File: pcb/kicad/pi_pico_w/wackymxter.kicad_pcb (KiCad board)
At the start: 2 copper layers, 165.9 x 126.4 mm, 73 parts, among them J1 OLED_128x32, U1 RP2040_Zero, U3 TRRS

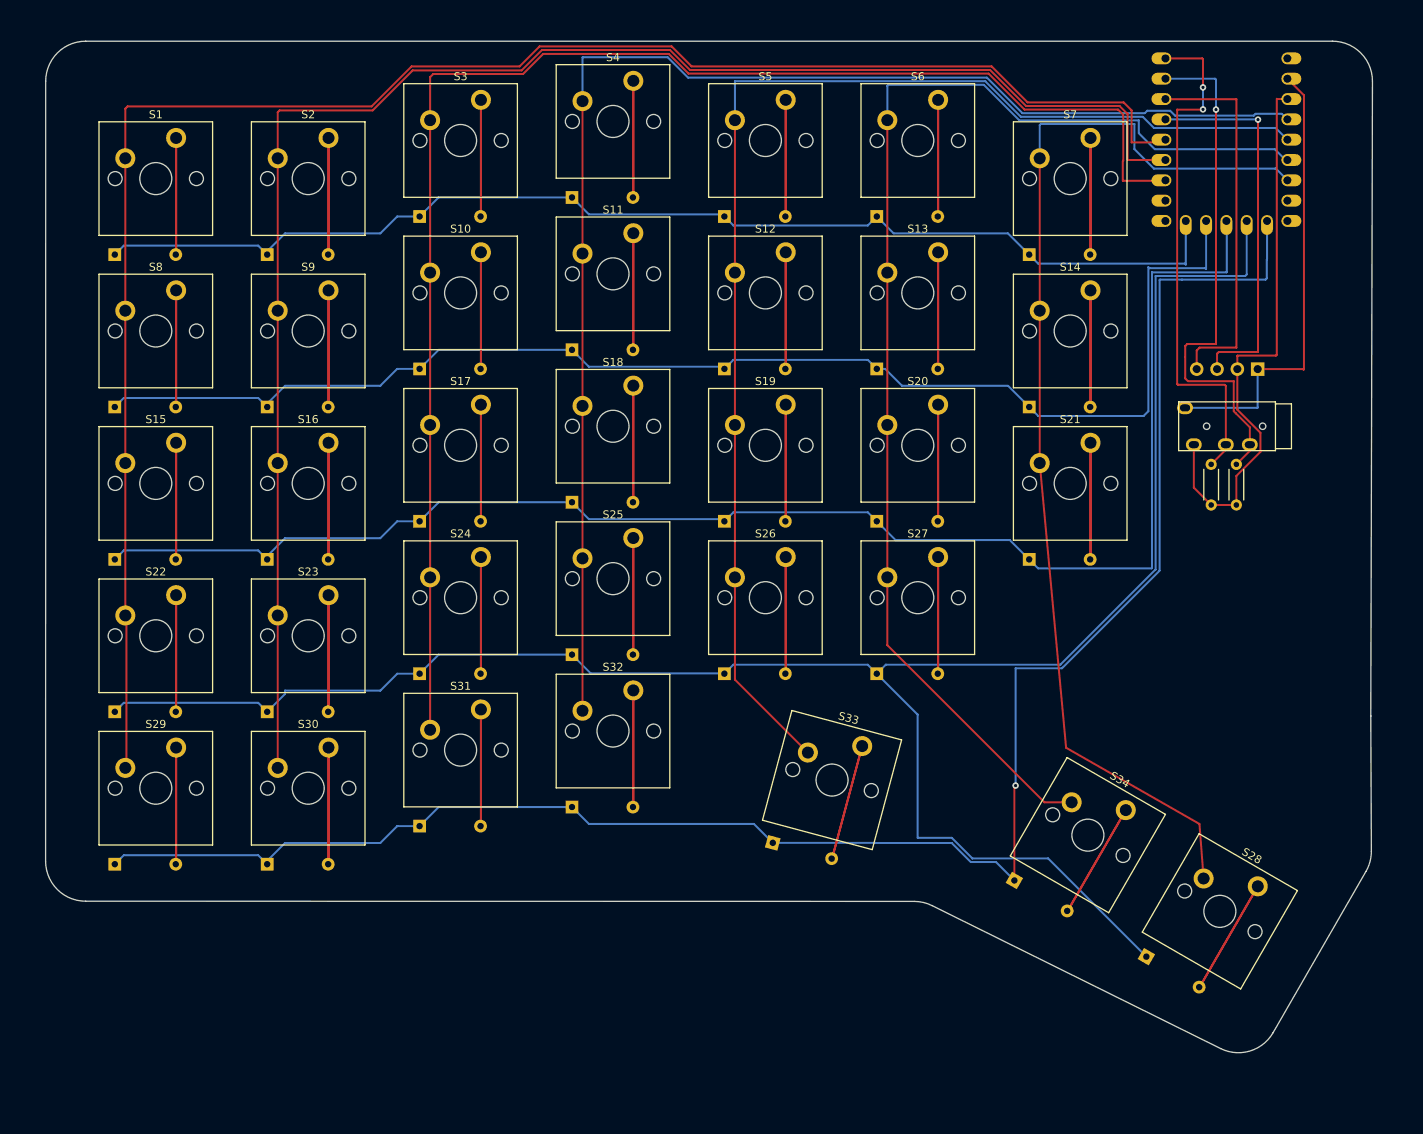
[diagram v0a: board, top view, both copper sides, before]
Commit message: [KiCAD] Pi Pico W with LEDs and Rotary Encoder
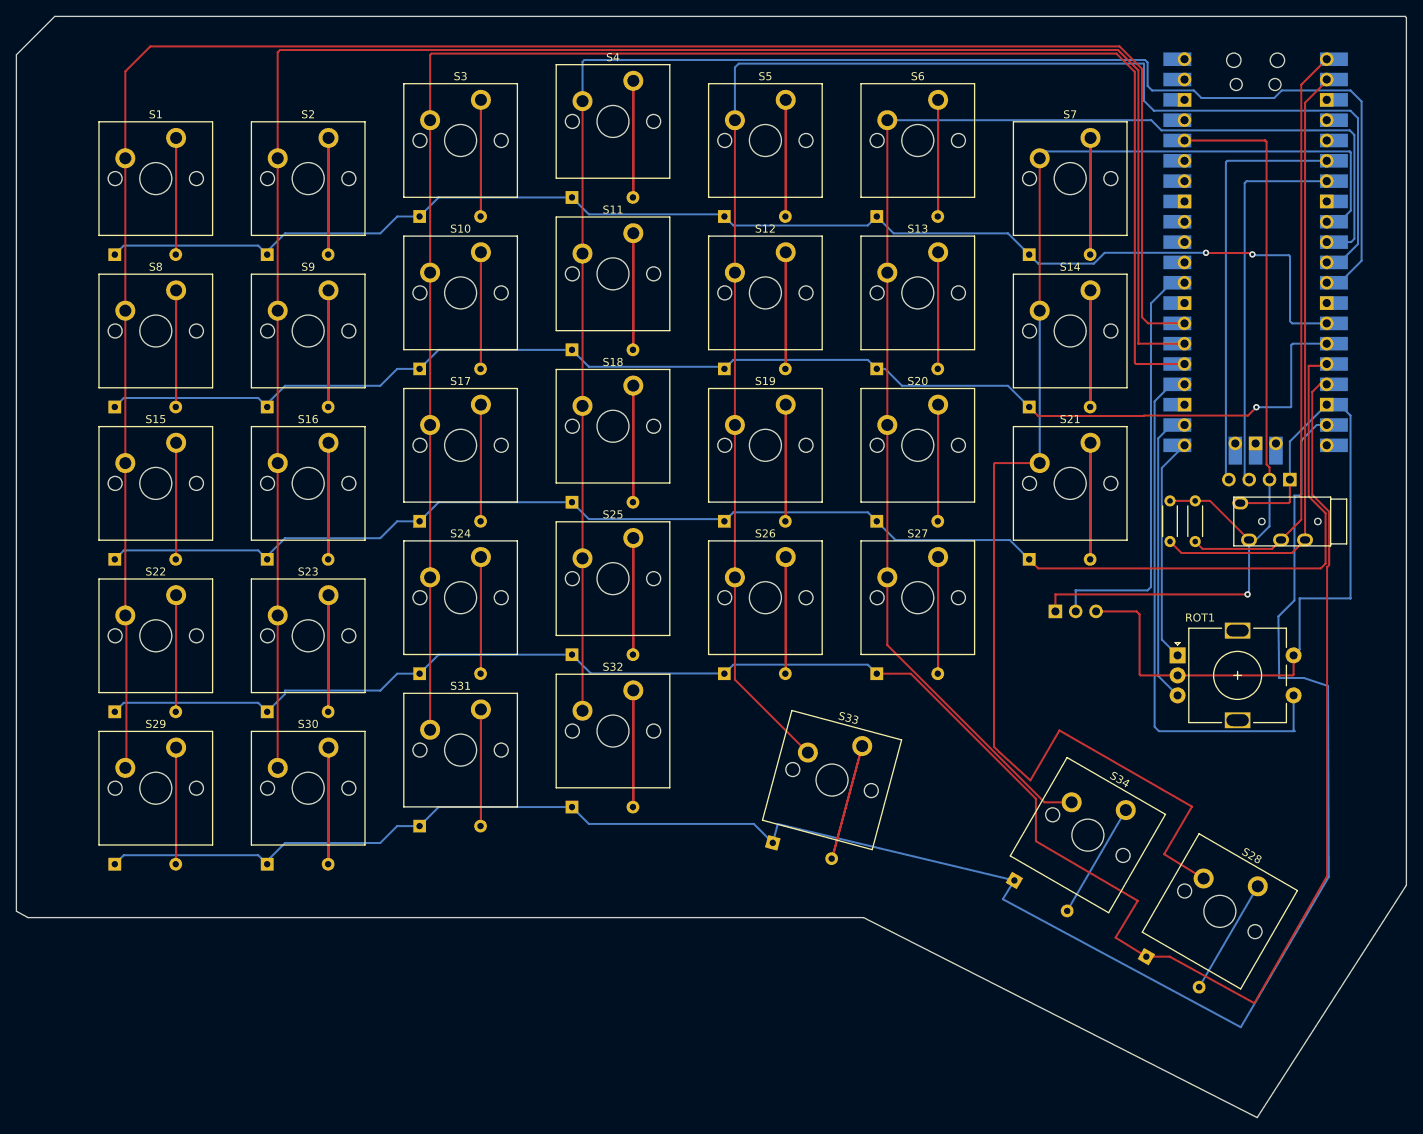
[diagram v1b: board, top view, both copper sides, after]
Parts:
- added J2: Conn_01x03, Connector_PinHeader_2.54mm:PinHeader_1x03_P2.54mm_Horizontal, B.Cu at (156.5, 95.8)
- added ROT1: RotaryEncoder_Switch, Rotary_Encoder:RotaryEncoder_Alps_EC11E-Switch_Vertical_H20mm, F.Cu at (171.8, 101.3)
- U1: value RP2040_Zero -> Pico; footprint ScottoKeebs_MCU:RP2040_Zero -> MCU_RaspberryPi_and_Boards:RPi_Pico_SMD_TH
- moved U1 14.5 mm to (181.5, 50.9)
- moved J1 14.4 mm to (176.0, 80.9)
- moved U3 13.8 mm to (190.9, 84.5)
- moved R2 8.31 mm to (170.8, 82.0), turned to -90 degrees
- moved R1 2.06 mm to (174.0, 82.0), turned to -90 degrees
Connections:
- U1 pad 10: row0 -> col5
- U1 pad 11: row1 -> col4
- U1 pad 12: row2 -> col3
- U1 pad 13: row3 -> unconnected-(U1-GND-Pad13)
- U1 pad 14: row4 -> row0
- U1 pad 15: unconnected-(U1-14-Pad15) -> row1
- U1 pad 16: unconnected-(U1-15-Pad16) -> row2
- U1 pad 17: col6 -> row3
- U1 pad 18: col5 -> GND
- U1 pad 19: col4 -> row4
- U1 pad 20: col3 -> unconnected-(U1-GPIO15-Pad20)
- U1 pad 21: VCC -> ROT1
- U1 pad 22: GND -> ROT2
- U1 pad 3: SDA -> unconnected-(U1-GND-Pad3)
- U1 pad 4: SCL -> unconnected-(U1-GPIO2-Pad4)
- U1 pad 5: col0 -> unconnected-(U1-GPIO3-Pad5)
- U1 pad 6: col1 -> SDA
- U1 pad 7: col2 -> SCL
- U1 pad 9: unconnected-(U1-8-Pad9) -> col6
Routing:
- net B1: track 0.00 -> 67.6 mm
- net LED1: track 0.00 -> 52.9 mm
- net GND: track 56.9 -> 95.4 mm
- net ROT2: track 0.00 -> 37.1 mm
- net VCC: track 71.0 -> 106.8 mm, vias 0 -> 1
- net col3: track 173.4 -> 208.6 mm
- net col6: track 139.8 -> 174.6 mm
- net col4: track 159.8 -> 193.6 mm
- net col1: track 205.2 -> 238.1 mm
- net col0: track 223.2 -> 253.4 mm
- net col2: track 186.2 -> 216.1 mm
- net ROT1: track 0.00 -> 28.3 mm
- net row0: track 147.9 -> 168.9 mm, vias 0 -> 2
- net row4: track 227.0 -> 244.8 mm, vias 1 -> 0
- net col5: track 156.0 -> 172.6 mm
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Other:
- board size 165.9 x 126.4 mm -> 173.8 x 137.6 mm
